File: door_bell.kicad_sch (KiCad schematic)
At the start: 79 parts, among them J1 Power, J2 Speaker, J3 SWITCH1, J4 UART, J5 MicroSD, J6 Door panel, K1 HJR 1-2C, Q1 BC847, SW1 Reset, SW2 Boot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

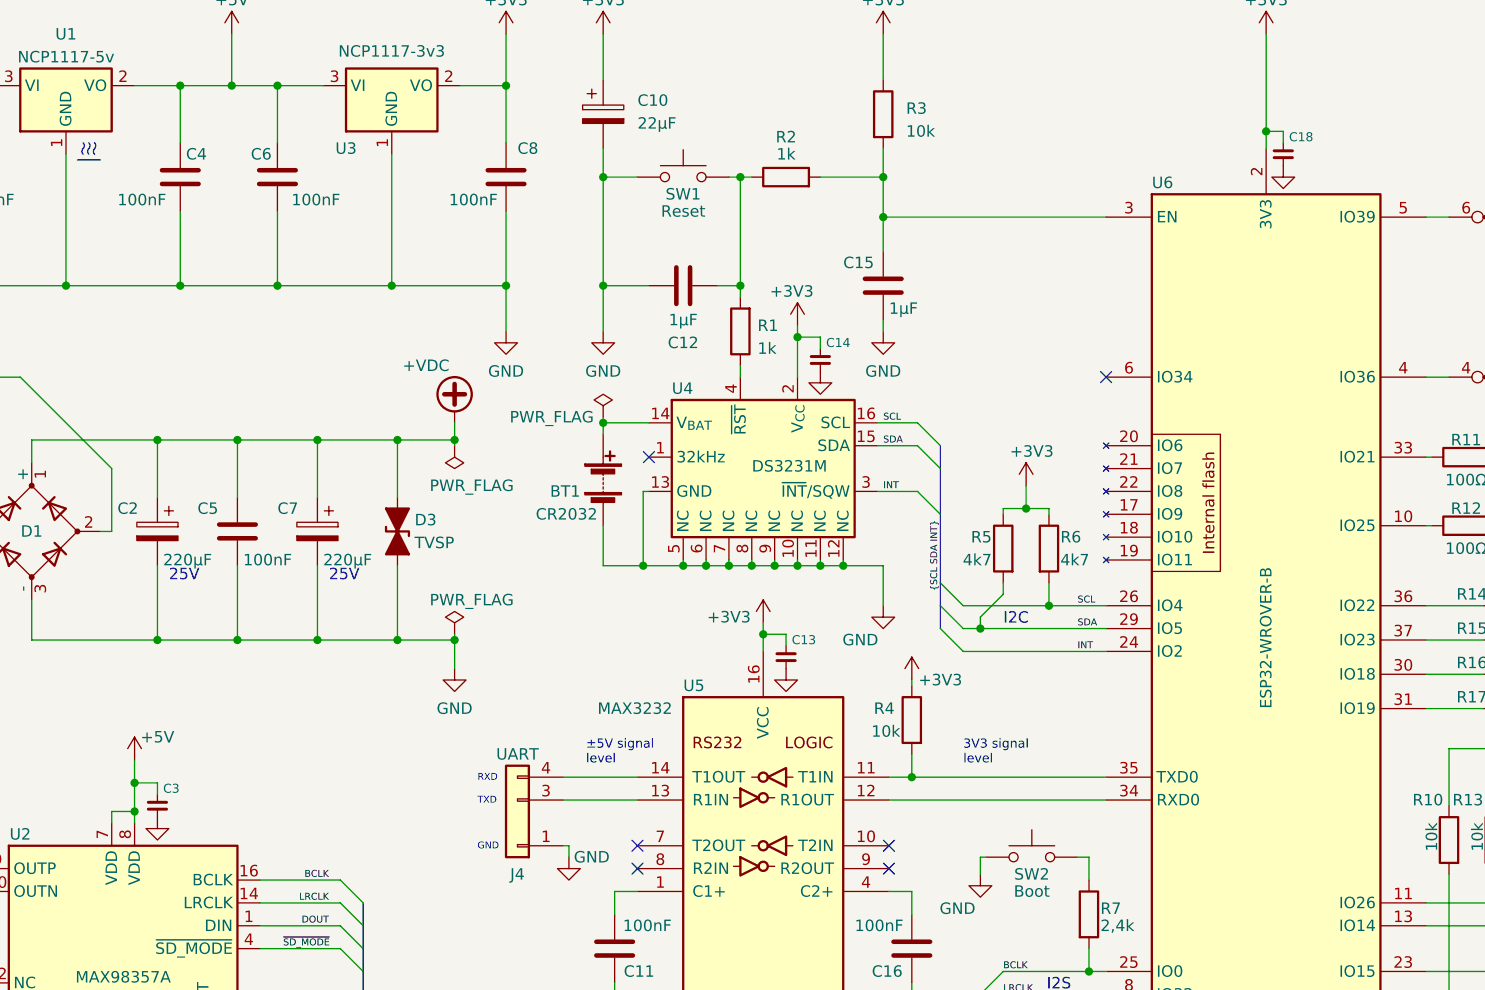
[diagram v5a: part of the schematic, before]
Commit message: Display values for decoupling capacitors
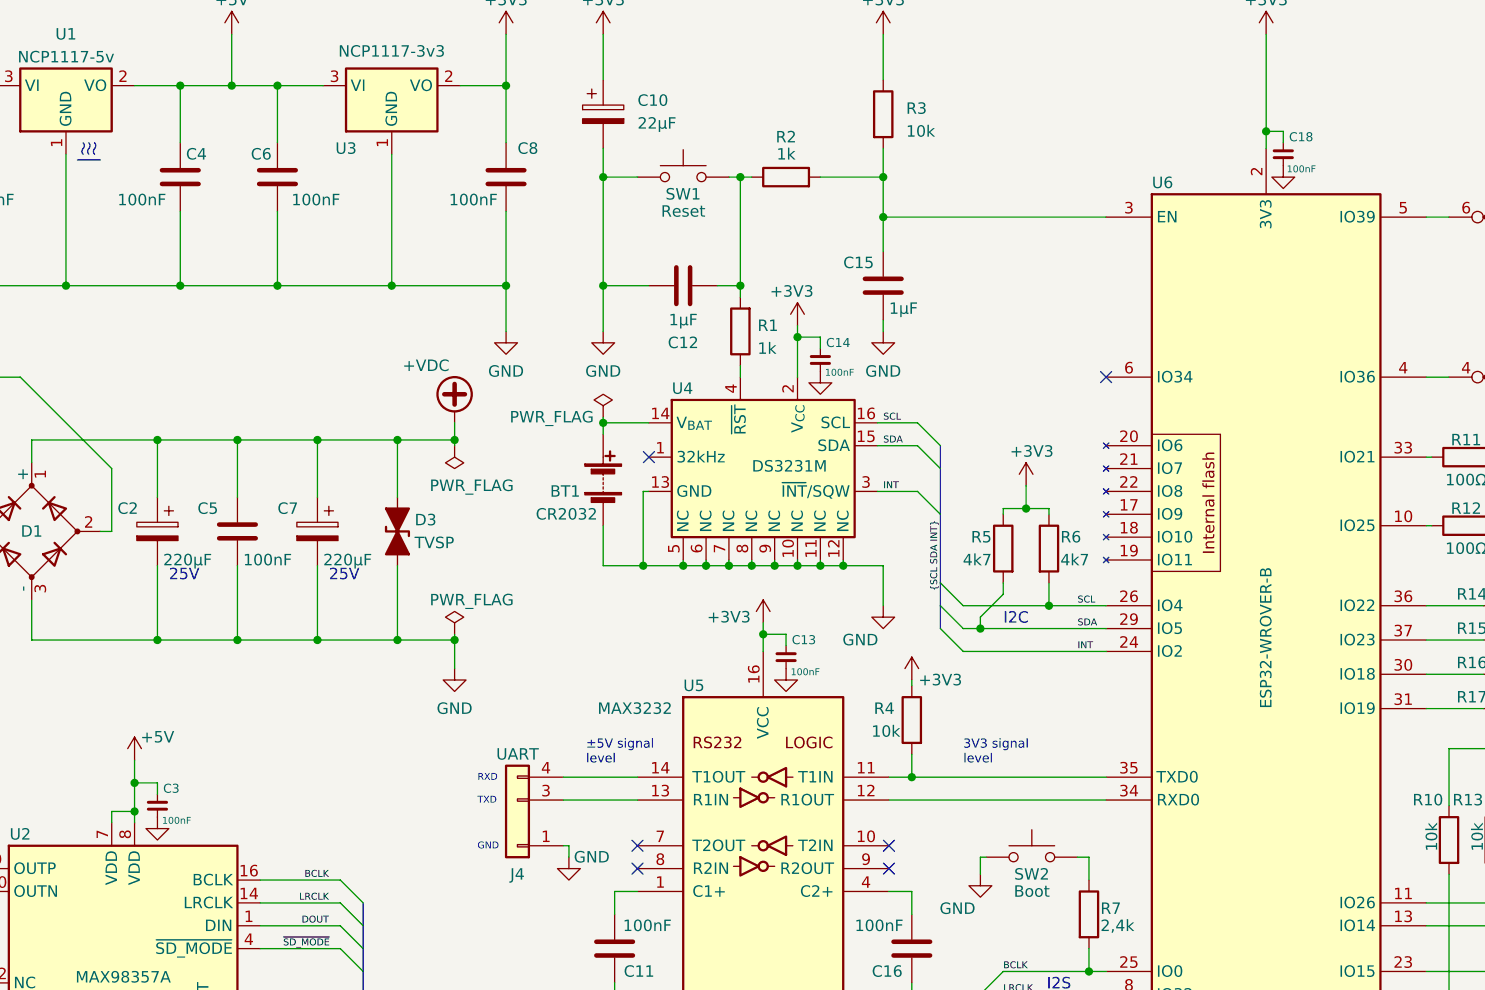
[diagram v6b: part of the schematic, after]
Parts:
- C13, C14, C18, C3: value C_Decoupling -> 100nF
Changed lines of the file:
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@@
       (effects (font (size 1 1)) (justify left))
     )
-    (property "Value" "C_Decoupling" (at 178.689 38.227 0)
-      (effects (font (size 1.27 1.27)) (justify left) hide)
+    (property "Value" "100nF" (at 178.816 37.846 0)
+      (effects (font (size 0.762 0.762)) (justify left))
     )
     (property "Footprint" "Capacitor_SMD:C_0805_2012Metric_Pad1.18x1.45mm_HandSolder" (at 178.435 36.195 0)
@@
       (effects (font (size 1 1)) (justify left))
     )
-    (property "Value" "C_Decoupling" (at 123.444 94.107 0)
-      (effects (font (size 1.27 1.27)) (justify left) hide)
+    (property "Value" "100nF" (at 123.698 93.726 0)
+      (effects (font (size 0.762 0.762)) (justify left))
     )
     (property "Footprint" "Capacitor_SMD:C_0805_2012Metric_Pad1.18x1.45mm_HandSolder" (at 123.19 92.075 0)
@@
     )
   )
-  (symbol (lib_id "Device_espena:C_Decoupling") (at 127 59.055 0) (mirror x) (unit 1)
+  (symbol (lib_name "C_Decoupling_1") (lib_id "Device_espena:C_Decoupling") (at 127 59.055 0) (mirror x) (unit 1)
     (in_bom yes) (on_board yes) (dnp no)
     (property "Reference" "C14" (at 127.635 57.15 0)
       (effects (font (size 1 1)) (justify left))
     )
-    (property "Value" "C_Decoupling" (at 127.254 57.023 0)
-      (effects (font (size 1.27 1.27)) (justify left) hide)
+    (property "Value" "100nF" (at 127.508 60.452 0)
+      (effects (font (size 0.762 0.762)) (justify left))
     )
     (property "Footprint" "Capacitor_SMD:C_0805_2012Metric_Pad1.18x1.45mm_HandSolder" (at 127 59.055 0)
@@
       (effects (font (size 1 1)) (justify left))
     )
-    (property "Value" "C_Decoupling" (at 53.594 110.617 0)
-      (effects (font (size 1.27 1.27)) (justify left) hide)
+    (property "Value" "100nF" (at 53.848 110.236 0)
+      (effects (font (size 0.762 0.762)) (justify left))
     )
     (property "Footprint" "Capacitor_SMD:C_0805_2012Metric_Pad1.18x1.45mm_HandSolder" (at 53.34 108.585 0)

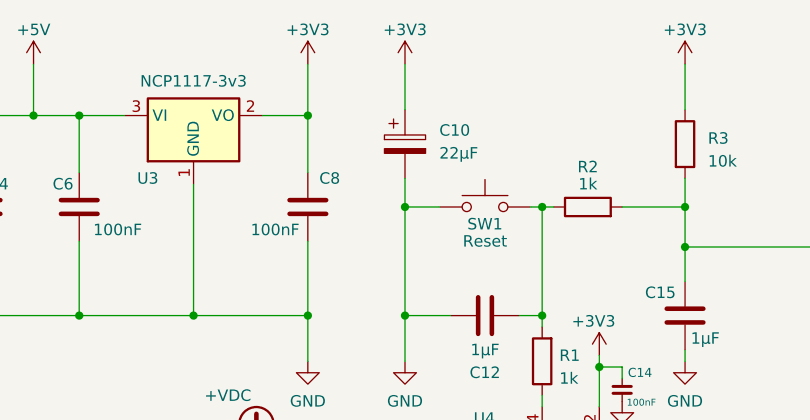
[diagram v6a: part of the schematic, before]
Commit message: Change C10 to non-polarized
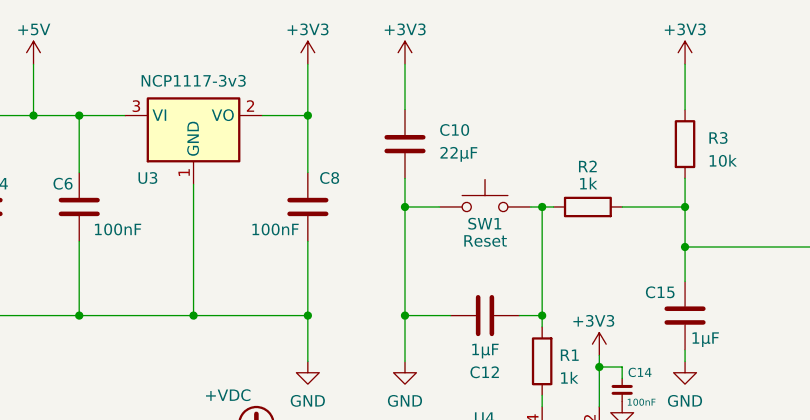
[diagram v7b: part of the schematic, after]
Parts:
- C10: symbol Device:C_Polarized -> Device:C
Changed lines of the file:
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@@
     )
   )
-  (symbol (lib_id "Device:C_Polarized") (at 102.87 31.75 0) (unit 1)
+  (symbol (lib_id "Device:C") (at 102.87 31.75 0) (unit 1)
     (in_bom yes) (on_board yes) (dnp no) (fields_autoplaced)
     (property "Reference" "C10" (at 106.68 30.226 0)
